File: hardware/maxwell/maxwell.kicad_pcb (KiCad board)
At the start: 2 copper layers, 129.5 x 59.7 mm, 89 parts, among them J1 Canbus 1, J2 Canbus 2, J3 Neopixel, J4 Boot Selection Jumper, J5 Charger Output, J6 Programmer, J7 Dynamo Input, J8 USB Input, J9 Battery, Q1 BSS138, Q2 Q_NMOS_GDS, Q3 Q_PMOS_GDS, U1 MCP2515-E/ST-SOIC, U10 LT1529, U11 TPS2514, U2 SN65HVD233, U3 ITEAD_HC-05, U4 SIM800L_5-pin, U5 BOOST_BOARD, U6 STT3P2UH7, U7 STM32F103RETx, U8 TLP188, U9 Buck Regulator, Y1 16M, Y2 8M, Y3 32.768k

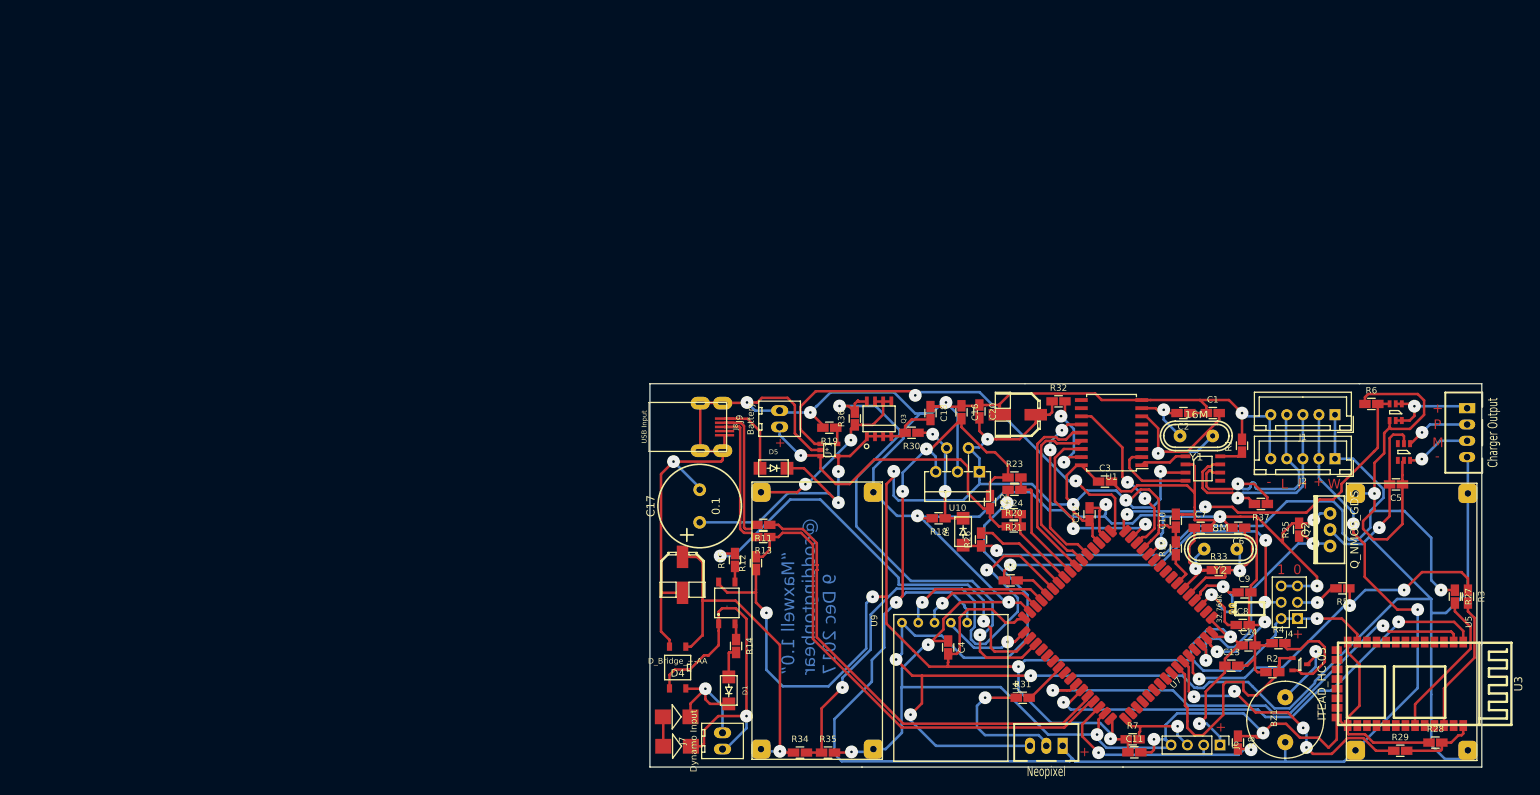
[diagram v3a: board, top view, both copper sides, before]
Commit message: Maxwell Board v2.0;
Adds:

* On-board P-MOS polarity protection.
* Adds On-board GPS (PA6C)
* Adds On-board WIFI, and BLE (ESP32)
* Connectors for 2x external UART devices.
* Connectors for 2x external SPI devices.
* Connector for I2C devices.

Removals:

* Removes on-board GSM; will add later via UART connectors mentioned
  above.
* Removes on-board boost charging.  Can later add this functionality via
  provided connectors.

Changes:

* Although the GNDPWR ground reference still exists, only neopixels
  are switched off via it.  The quiescent current of the GPS module
  and the ESP32 can be controlled via other means.
* Swaps many of the ICs used for switching and power regulation.
* Removes boot jumper bank.  I very rarely used it, and the HC-05
  has now been proven to work for switching boot modes for remote
  flashing.
* Removes natural powered-off state previously handled bydisabling the
  voltage regulator until POWER_ON was pulled high.  This will
  undoubtedly decrease how long the device will be able to operate due
  to increased quiescent currents, but I am willing to accept that given
  that removing that logic makes the design and software (especially
  around keeping the device on while flashing) simpler.
* Many other minor things.
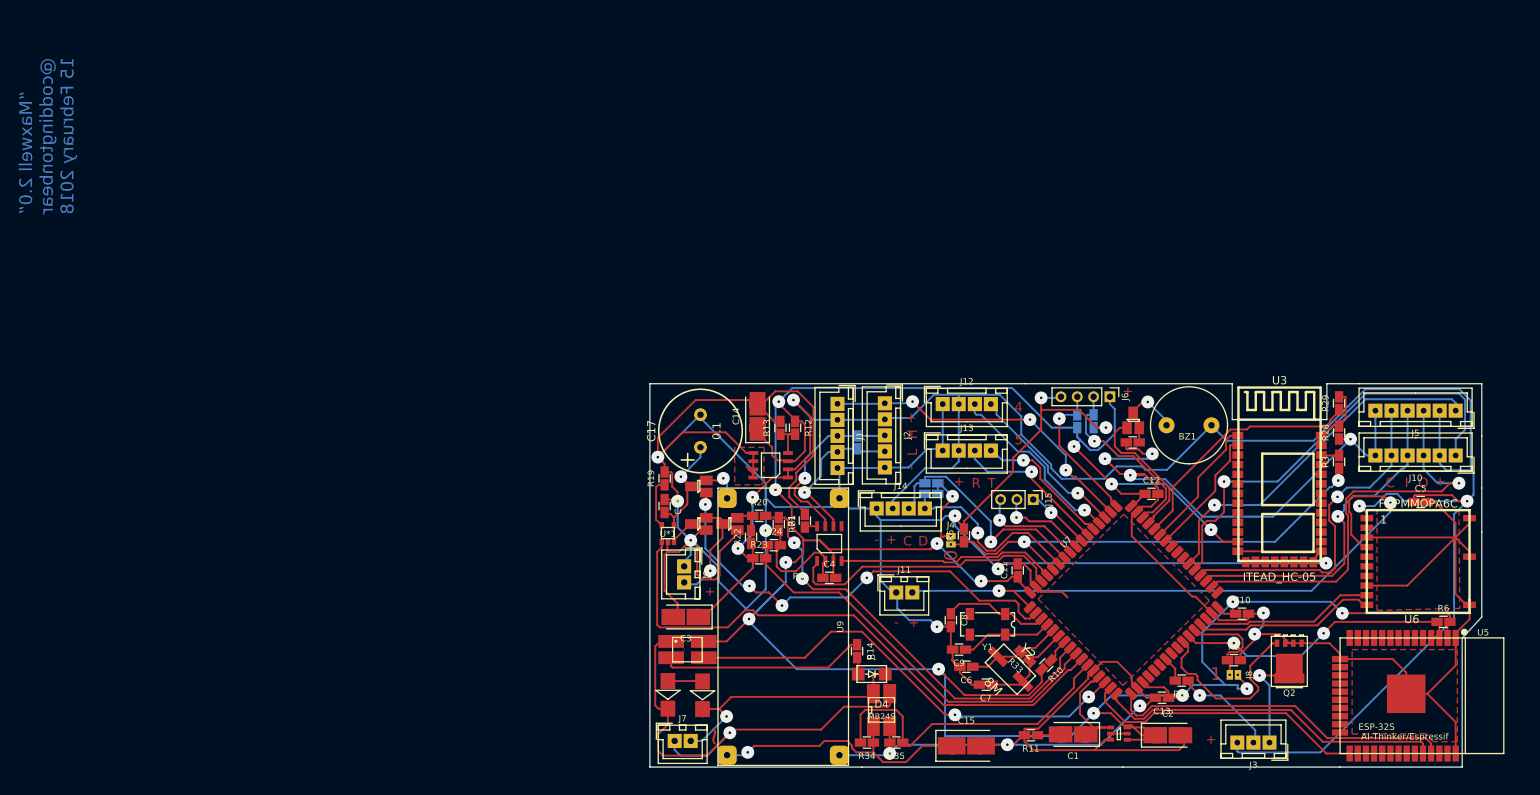
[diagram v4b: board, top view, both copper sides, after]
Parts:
- removed C16: 100nF, coddingtonbear/coddingtonbear.pretty:0805_Milling
- removed C19: 220u, xesscorp/xess.pretty:xess-ECAP-SMT-6.3MM
- removed C20: 100n, coddingtonbear/coddingtonbear.pretty:0805_Milling
- removed D5, D6: D, mcous/kicad-lib/footprints/diode.pretty:DO-214AC
- removed R15: 330, coddingtonbear/coddingtonbear.pretty:0805_Milling
- removed R18, R25: 100k, coddingtonbear/coddingtonbear.pretty:0805_Milling
- removed R26, R27: 1k, coddingtonbear/coddingtonbear.pretty:0805_Milling
- removed R30: 1.5k, coddingtonbear/coddingtonbear.pretty:0805_Milling
- removed R32, R36: 10k, coddingtonbear/coddingtonbear.pretty:0805_Milling
- removed U11: TPS2514, adamgreig/agg-kicad/agg.pretty:SOT-23-6
- removed U4: SIM800L_5-pin, coddingtonbear/coddingtonbear.pretty:SIM800L_Breakout
- removed Y3: 32.768k, f4grx/f4libs_th.pretty:XTAL32K
- added J10: SPI2_B, coddingtonbear/coddingtonbear.pretty:JST_XH_B06B-XH-A_06x2.50mm_Straight_LargePads, F.Cu at (199.1, 82.3)
- added J11: BACKUP, coddingtonbear/coddingtonbear.pretty:JST_XH_B02B-XH-A_02x2.50mm_Straight_LargePads, F.Cu at (112.0, 103.6)
- added J12: UART4, coddingtonbear/coddingtonbear.pretty:JST_XH_B04B-XH-A_04x2.50mm_Straight_LargePads, F.Cu at (119.3, 74.3)
- added J13: UART5, coddingtonbear/coddingtonbear.pretty:JST_XH_B04B-XH-A_04x2.50mm_Straight_LargePads, F.Cu at (119.3, 81.5)
- added J14: I2C1, coddingtonbear/coddingtonbear.pretty:JST_XH_B04B-XH-A_04x2.50mm_Straight_LargePads, F.Cu at (109.0, 90.6)
- added J15: GPIO, KiCad/Pin_Headers.pretty:Pin_Header_Straight_1x03_Pitch2.54mm, F.Cu at (133.3, 89.2)
- added Q4: NTR1P02T1, coddingtonbear/coddingtonbear.pretty:SOT-23_LargePads, F.Cu at (81.3, 93.0)
- added Q5: NTR1P02T1, coddingtonbear/coddingtonbear.pretty:SOT-23_LargePads, F.Cu at (86.1, 93.0)
- added R16: 2.2k, coddingtonbear/coddingtonbear.pretty:0805_Milling, B.Cu at (117.5, 88.3)
- C1, C2: value 22p -> 2.2u; footprint coddingtonbear/coddingtonbear.pretty:0805_Milling -> coddingtonbear:CP_Tantalum_Case-C_EIA-6032-28_Milling
- C14: value 100n -> 220u; footprint coddingtonbear/coddingtonbear.pretty:0805_Milling -> coddingtonbear:CP_Tantalum_Case-C_EIA-6032-28_Milling
- C15: footprint xesscorp/xess.pretty:xess-ECAP-SMT-6.3MM -> coddingtonbear:CP_Tantalum_Case-D_EIA-7343-31_Milling
- C3: value 0.1u -> 2.2u; footprint coddingtonbear/coddingtonbear.pretty:0805_Milling -> coddingtonbear:CP_Tantalum_Case-C_EIA-6032-28_Milling
- D4: value D_Bridge_+-AA -> MB24S; footprint ep092/library_toni.pretty:SO-4 -> coddingtonbear/coddingtonbear.pretty:SO-4_Milling
- J1, J2: footprint KiCad/Connectors_JST.pretty:JST_XH_B05B-XH-A_05x2.50mm_Straight -> coddingtonbear/coddingtonbear.pretty:JST_XH_B05B-XH-A_05x2.50mm_Straight_LargePads
- J3: footprint pbrook/Parts.pretty:JST-XH-3 -> coddingtonbear/coddingtonbear.pretty:JST_XH_B03B-XH-A_03x2.50mm_Straight_LargePads
- J4: value Boot Selection Jumper -> BOOT0; footprint KiCad/Pin_Headers.pretty:Pin_Header_Straight_2x03_Pitch2.54mm -> coddingtonbear:Pin_Header_Straight_1x02_Pitch1.27mm_JMP
- J5: value Charger Output -> SPI2_A; footprint pbrook/Parts.pretty:JST-XH-4 -> coddingtonbear/coddingtonbear.pretty:JST_XH_B06B-XH-A_06x2.50mm_Straight_LargePads
- J7, J9: footprint ChristianLerche/LercheTech_KiCAD/LercheTech.pretty:Lerche_2P_2.54mm_Terminal -> coddingtonbear/coddingtonbear.pretty:JST_XH_B02B-XH-A_02x2.50mm_Straight_LargePads
- J8: value USB Input -> BOOT1; footprint coddingtonbear/coddingtonbear.pretty:UJ2-MIBH-4-SMT -> coddingtonbear:Pin_Header_Straight_1x02_Pitch1.27mm_JMP
- Q1: footprint adamgreig/agg-kicad/agg.pretty:SOT-23 -> coddingtonbear/coddingtonbear.pretty:SOT-23_LargePads
- Q2: value Q_NMOS_GDS -> PSMN5R4-25YLD; footprint fruchti/fruchtilib/mod/to.pretty:TO220 -> coddingtonbear/coddingtonbear.pretty:PSMN5R4-25YLD
- Q3: value Q_PMOS_GDS -> NTR1P02T1; footprint coddingtonbear/coddingtonbear.pretty:NDS8434 -> coddingtonbear/coddingtonbear.pretty:SOT-23_LargePads
- R11: value 20 -> 50
- R12: value 1.5k -> 16-17k
- R13: value 20 -> 10k
- R14: value 330 -> 200
- R2: value 10k -> 2.2k; moved to B.Cu
- R20, R23: value 4.7k -> ANY
- R21, R24: value 10k -> ANY
- R34: value 10k -> 110k
- R35: value 2k -> 10k
- R37, R7, R8: moved to B.Cu
- R6: value 100k -> 10k
- U1: value MCP2515-E/ST-SOIC -> MCP1501; footprint Tinkerforge/kicad-libraries:SOIC-18 -> adamgreig/agg-kicad/agg.pretty:SOT-23-6
- U10: value LT1529 -> MIC39102; footprint KiCad/TO_SOT_Packages_THT.pretty:TO-220-5_Pentawatt_Multiwatt-5_Vertical_StaggeredType2 -> adamgreig/agg-kicad/agg.pretty:SOIC-8
- U5: value BOOST_BOARD -> ESP-32S; footprint coddingtonbear/coddingtonbear.pretty:BOOST_LM2596_3A -> coddingtonbear/coddingtonbear.pretty:ESP-32S
- U6: value STT3P2UH7 -> FGPMMOPA6C; footprint adamgreig/agg-kicad/agg.pretty:SOT-23-6 -> coddingtonbear/coddingtonbear.pretty:FGPMMOPA6C
- U8: footprint Tinkerforge/kicad-libraries:SO-4 -> coddingtonbear/coddingtonbear.pretty:SO-4_Milling
- Y1: value 16M -> 32.768k; footprint SchrodingersGat/Components.pretty:crystal_hc-49s -> KiCad/Crystals.pretty:Crystal_SMD_SeikoEpson_MC306-4pin_8.0x3.2mm
- Y2: footprint SchrodingersGat/Components.pretty:crystal_hc-49s -> nqbit/NQBit.pretty:HC-49USX_SMD
- moved J8 88.5 mm to (165.2, 116.5)
- moved C14 84.4 mm to (90.4, 76.2), turned to 90 degrees
- moved J1 77.5 mm to (102.9, 74.2), turned to 270 degrees
- moved J2 70.6 mm to (110.2, 74.2), turned to 270 degrees
- moved R1 69.1 mm to (97.8, 92.4)
- moved C3 68.6 mm to (79.2, 107.4), turned to 180 degrees
- moved R37 63.6 mm to (105.9, 80.2), turned to 90 degrees
- moved R2 60.7 mm to (117.5, 86.6), turned to 180 degrees
- moved R5 59.5 mm to (122.6, 94.7), turned to 90 degrees
- moved U2 59.3 mm to (101.6, 96.0), turned to 90 degrees
- moved J6 56.9 mm to (145.3, 73.2)
- moved J4 55.5 mm to (120.5, 94.9), turned to 0 degrees
- moved R29 54.9 mm to (181.0, 74.2), turned to 90 degrees
- moved R8 54.9 mm to (142.7, 77.0), turned to 90 degrees
- moved C1 54.6 mm to (139.6, 125.7), turned to 180 degrees
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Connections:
- net RXD renamed BT_DO
- net TXD renamed BT_DI
- C1 pad 1: GND -> Net-(C1-Pad1)
- C2 pad 1: Net-(C2-Pad1) -> +3V3
- C2 pad 2: Net-(C2-Pad2) -> GND
- C3 pad 1: +3V3 -> +BATT
- C5 pad 1: Net-(C5-Pad1) -> +BATT
- C5 pad 2: GNDPWR -> GND
- J3 pad 1: +BATT -> GNDPWR
- J3 pad 3: GNDPWR -> +BATT
- J4 pad 2: +3V3 -> BOOT0
- J5 pad 1: Net-(J5-Pad1) -> SPI2_CS_A
- J5 pad 2: Net-(J5-Pad2) -> +BATT
- J5 pad 3: Net-(J5-Pad3) -> SPI2_MOSI
- J5 pad 4: GNDPWR -> SPI2_MISO
- J8 pad 1: Net-(D5-Pad2) -> +3V3
- J8 pad 2: USB- -> BOOT1
- J9 pad 1: Net-(J9-Pad1) -> GND
- J9 pad 2: GND -> Net-(J9-Pad2)
- Q2 pad 1: ENABLE_BATT_POWER -> GND
- Q2 pad 2: GNDPWR -> ENABLE_BATT_POWER
- Q2 pad 3: GND -> GNDPWR
- Q3 pad 2: /Power/+Dynamo -> Net-(Q3-Pad2)
- Q3 pad 3: Net-(Q3-Pad3) -> /Power/+Dynamo
- R11 pad 1: /Microcontroller/USB_PRER- -> Net-(C1-Pad2)
- R11 pad 2: USB- -> GND
- R12 pad 2: /Microcontroller/USB_PRER+ -> Net-(R12-Pad2)
- R13 pad 1: /Microcontroller/USB_PRER+ -> Net-(R12-Pad2)
- R13 pad 2: USB+ -> GND
- R2 pad 1: GND -> +3V3
- R2 pad 2: BUZZER -> I2C1_SCL
- R20 pad 1: Net-(J9-Pad1) -> Net-(Q5-Pad2)
- R21 pad 2: GNDPWR -> GND
- R22 pad 2: Net-(J9-Pad1) -> Net-(Q5-Pad2)
- R24 pad 2: GNDPWR -> GND
- R5 pad 2: Net-(J4-Pad3) -> GND
- R6 pad 1: Net-(C5-Pad1) -> ~DISABLE_ESP
- R6 pad 2: ~ENABLE_USB_OUT -> +3V3
- R9 pad 1: Net-(J4-Pad4) -> BOOT1
- R9 pad 2: BOOT1 -> GND
- U*1 pad 3: Net-(J9-Pad1) -> Net-(Q4-Pad3)
- U1 pad 1: /TXCAN -> Net-(C1-Pad1)
- U1 pad 2: /RXCAN -> GND
- U1 pad 3: Net-(U1-Pad3) -> GND
- U1 pad 4: Net-(U1-Pad4) -> +3V3
- U1 pad 5: Net-(U1-Pad5) -> GND
- U1 pad 6: Net-(U1-Pad6) -> +3V3
- U10 pad 1: +3V3 -> +BATT
- U10 pad 2: +3V3 -> +BATT
- U10 pad 3: GND -> +3V3
- U10 pad 4: Net-(D6-Pad1) -> Net-(R12-Pad2)
- U10 pad 5: +BATT -> GND
- U2 pad 1: /TXCAN -> CAN_TX
- U2 pad 4: /RXCAN -> CAN_RX
- U5 pad 1: +BATT -> GND
- U5 pad 2: GNDPWR -> +3V3
- U5 pad 3: Net-(C5-Pad1) -> ~DISABLE_ESP
- U5 pad 4: GNDPWR -> Net-(U5-Pad4)
- U6 pad 1: Net-(J5-Pad1) -> +BATT
- U6 pad 3: ~ENABLE_USB_OUT -> GND
- U6 pad 4: Net-(C5-Pad1) -> +BACKUP
- U6 pad 5: Net-(J5-Pad1) -> Net-(U6-Pad5)
- U6 pad 6: Net-(J5-Pad1) -> Net-(U6-Pad6)
- U7 pad 1: +3V3 -> +BACKUP
- U7 pad 10: Net-(U7-Pad10) -> ~BATT_CHARGING
- U7 pad 11: Net-(U7-Pad11) -> DYNAMO_VOLTAGE
- U7 pad 13: +3V3 -> Net-(C1-Pad1)
- U7 pad 14: CAN_INT -> SPEED
- U7 pad 15: ~CAN_CS -> ESP_BOOT_MODE
- U7 pad 16: ~ENABLE_USB_OUT -> ESP_DI
- U7 pad 17: ~BATT_CHARGING -> ESP_DO
- U7 pad 2: Net-(U7-Pad2) -> ~BATT_CHARGE_ENABLE
- U7 pad 21: SCK -> Net-(U7-Pad21)
- U7 pad 22: MISO -> Net-(U7-Pad22)
- U7 pad 23: MOSI -> NEOPIXEL
- U7 pad 24: CURRENT_SENSE -> Net-(U7-Pad24)
- U7 pad 25: BATT_VOLTAGE -> Net-(U7-Pad25)
- U7 pad 26: Net-(R26-Pad2) -> ENABLE_BATT_POWER
- U7 pad 27: DYNAMO_VOLTAGE -> ~DISABLE_ESP
- U7 pad 29: GSM_TXD -> GPS_DI
- U7 pad 30: GSM_RXD -> GPS_DO
- U7 pad 33: GSM_RST -> Net-(U7-Pad33)
- U7 pad 34: SPEED -> SPI2_MOSI
- U7 pad 35: ~BATT_CHARGE_ENABLE -> SPI2_MISO
- U7 pad 36: Net-(U7-Pad36) -> SPI2_SCK
- U7 pad 37: Net-(U7-Pad37) -> SPI2_CS_B
- U7 pad 38: Net-(U7-Pad38) -> SPI2_CS_A
- U7 pad 39: NEOPIXEL -> Net-(U7-Pad39)
- U7 pad 44: /Microcontroller/USB_PRER- -> BT_KEY
- U7 pad 45: /Microcontroller/USB_PRER+ -> BUZZER
- U7 pad 50: Net-(U7-Pad50) -> POWER_ON
- U7 pad 51: Net-(U7-Pad51) -> UART4_TX
- U7 pad 52: Net-(U7-Pad52) -> UART4_RX
- U7 pad 53: Net-(U7-Pad53) -> UART5_TX
- U7 pad 54: Net-(U7-Pad54) -> UART5_RX
- U7 pad 58: BUZZER -> I2C1_SCL
- U7 pad 59: BT_KEY -> I2C1_SDA
- U7 pad 61: Net-(U7-Pad61) -> CAN_RX
- U7 pad 62: ENABLE_BATT_POWER -> CAN_TX
- U7 pad 8: Net-(U7-Pad8) -> BATT_VOLTAGE
- U7 pad 9: Net-(U7-Pad9) -> CURRENT_SENSE
- U8 pad 4: Net-(R15-Pad1) -> SPEED
- U9 pad 3: Net-(Q3-Pad3) -> Net-(Q3-Pad2)
- Y1 pad 1: Net-(C1-Pad2) -> Net-(C8-Pad1)
- Y1 pad 2: Net-(C2-Pad2) -> Net-(Y1-Pad2)
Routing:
- net GNDPWR: track 280.2 -> 20.0 mm, vias 5 -> 1
- net GND: track 639.5 -> 839.4 mm
- net +BACKUP: track 0.00 -> 103.2 mm, vias 0 -> 2
- net /Microcontroller/USB_PRER+: track 77.9 -> 0.00 mm
- net /Microcontroller/USB_PRER-: track 73.1 -> 0.00 mm
- net +3V3: track 381.8 -> 453.0 mm, vias 12 -> 16
- net SPI2_CS_B: track 0.00 -> 70.4 mm, vias 0 -> 1
- net +BATT: track 252.1 -> 321.8 mm
- net SPI2_MOSI: track 0.00 -> 67.6 mm, vias 0 -> 1
- net POWER_ON: track 118.0 -> 51.6 mm, vias 2 -> 3
- net Net-(C5-Pad1): track 60.7 -> 0.00 mm, vias 1 -> 0
- net Net-(J4-Pad4): track 58.3 -> 0.00 mm, vias 3 -> 0
- net SPI2_CS_A: track 0.00 -> 56.6 mm, vias 0 -> 1
- net ~ENABLE_USB_OUT: track 56.5 -> 0.00 mm, vias 2 -> 0
- net BT_DI: track 75.8 -> 20.2 mm, vias 2 -> 0
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- added copper zone on F.Cu, net GND
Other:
- outline, holes or cut-outs redrawn
- net class Default: clearance 0.25 -> 0.2; trace_width 0.4 -> 0.3
- rule trace_clearance: 0.25 -> 0.2
- board text added: "4"
- board text added: "5"
- board text added: "C"
- board text added: "D"
- board text added: "I"
- board text added: "O"
- board text added: "R"
- board text added: "T"
- board text added: "~"
- board text added: "~~"
- board text added: "“Maxwell 2.0” @coddingtonbear 15 February 2018"
- board text removed: "M"
- board text removed: "P"
- board text removed: "W"
- board text removed: "“Maxwell 1.0” @coddingtonbear 9 Dec 2017"

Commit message: Adding label.
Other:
- board text added: "Maxwell v2.0 @coddingtonbear 17 February 2018"
- board text removed: "“Maxwell 2.0” @coddingtonbear 15 February 2018"
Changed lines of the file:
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@@
   (layers
     (0 F.Cu signal)
-    (31 B.Cu signal)
-    (33 F.Adhes user)
-    (35 F.Paste user)
-    (37 F.SilkS user)
-    (39 F.Mask user)
-    (40 Dwgs.User user)
-    (41 Cmts.User user)
-    (42 Eco1.User user)
-    (43 Eco2.User user)
-    (44 Edge.Cuts user)
-    (45 Margin user)
-    (47 F.CrtYd user)
-    (49 F.Fab user)
+    (31 B.Cu signal hide)
+    (33 F.Adhes user hide)
+    (35 F.Paste user hide)
+    (37 F.SilkS user hide)
+    (39 F.Mask user hide)
+    (40 Dwgs.User user hide)
+    (41 Cmts.User user hide)
+    (42 Eco1.User user hide)
+    (43 Eco2.User user hide)
+    (44 Edge.Cuts user hide)
+    (45 Margin user hide)
+    (47 F.CrtYd user hide)
+    (49 F.Fab user hide)
   )
   (setup
@@
     (pad_to_mask_clearance 0.2)
     (aux_axis_origin 73.66 130.81)
-    (visible_elements FFFFFF7F)
+    (visible_elements FFFFFD7F)
     (pcbplotparams
       (layerselection 0x01030_ffffffff)
@@
     (tags "resistor 0805")
     (attr smd)
-    (fp_text reference R5 (at 0 -2.1 90) (layer F.SilkS)
+    (fp_text reference R5 (at 2.286 1.905 90) (layer F.SilkS)
       (effects (font (size 1 1) (thickness 0.15)))
     )
@@
     (effects (font (size 1.5 1.5) (thickness 0.3)))
   )
-  (gr_text "“Maxwell 2.0”\n@coddingtonbear\n15 February 2018" (at -20.2565 44.7675 90) (layer B.Cu)
+  (gr_text "Maxwell v2.0\n@coddingtonbear\n17 February 2018" (at 129.286 110.236) (layer B.Cu)
     (effects (font (size 2 2) (thickness 0.25)) (justify right mirror))
   )

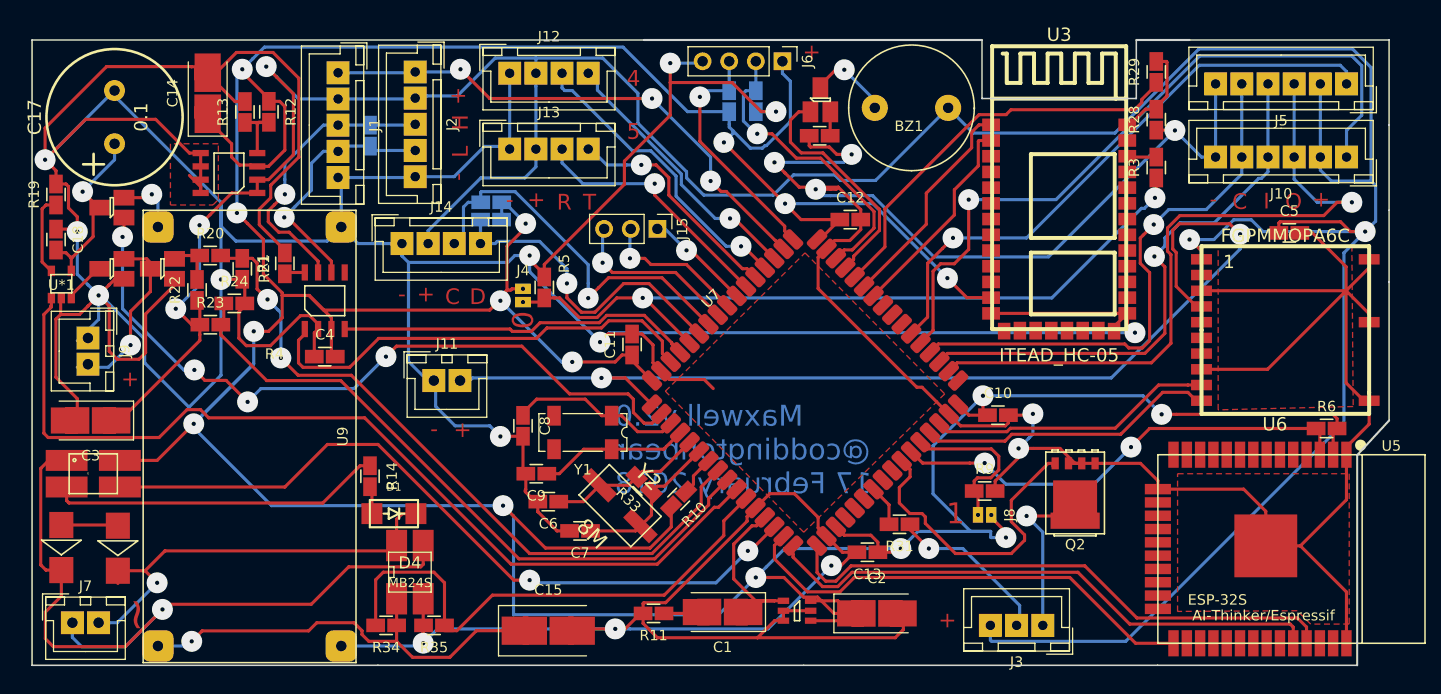
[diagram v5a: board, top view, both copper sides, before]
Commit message: Updating to use 0.4mm traces.
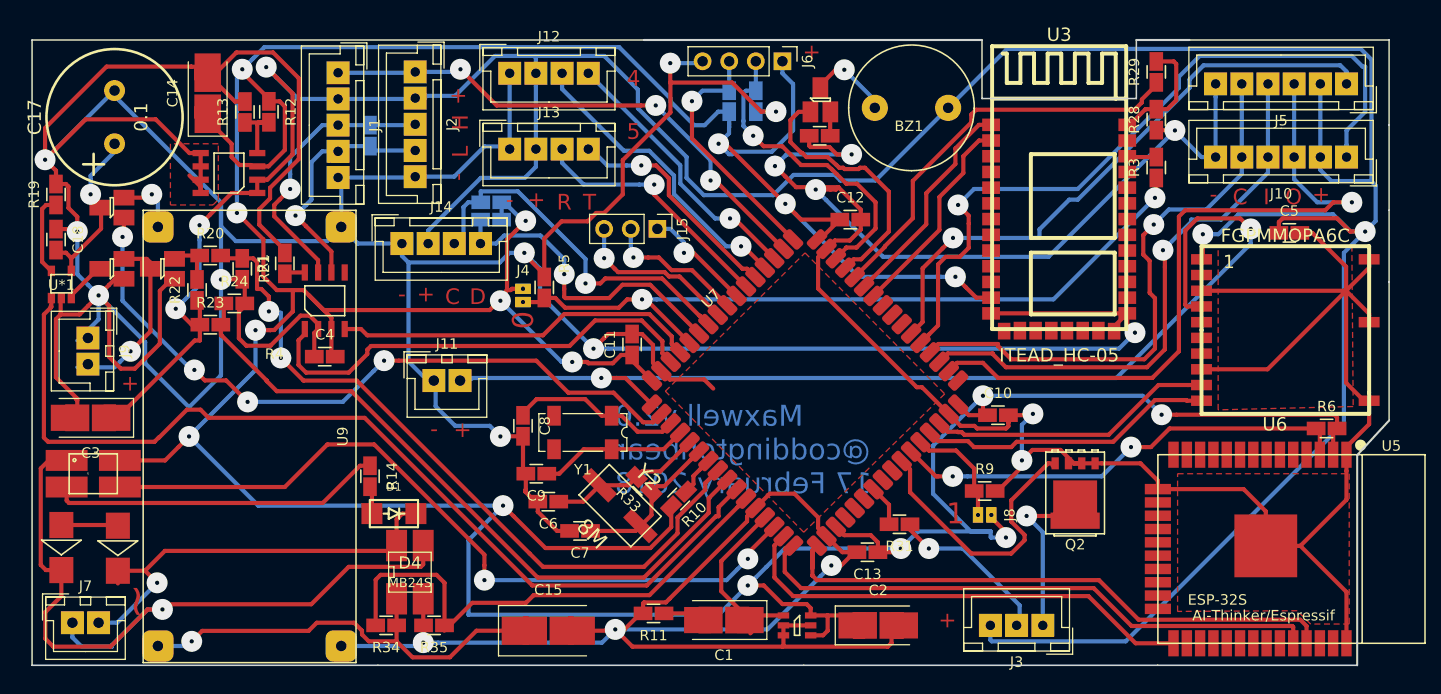
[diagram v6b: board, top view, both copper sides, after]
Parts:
- moved U1 1.40 mm to (146.7, 127.0)
- moved C2 1.15 mm to (154.4, 127.0)
- moved C1 0.77 mm to (139.7, 126.5)
- moved C3 0.25 mm to (79.2, 107.2)
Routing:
- net GND: track 839.4 -> 845.2 mm
- net BOOT1: track 16.0 -> 11.2 mm
- net BUZZER: track 22.4 -> 25.2 mm
- net ~BATT_CHARGING: track 89.8 -> 92.6 mm
- net ENABLE_BATT_POWER: track 29.9 -> 27.5 mm
- net ~BATT_CHARGE_ENABLE: track 70.2 -> 67.8 mm
- net BATT_VOLTAGE: track 68.0 -> 70.2 mm
- net SPI2_CS_B: track 70.4 -> 72.6 mm
- net CURRENT_SENSE: track 63.9 -> 65.9 mm
- net SPI2_SCK: track 52.7 -> 54.7 mm
- net SPI2_MOSI: track 67.6 -> 69.4 mm
- net Net-(R28-Pad2): track 9.35 -> 11.1 mm
- net I2C1_SCL: track 37.1 -> 35.5 mm
- net SPEED: track 71.8 -> 73.4 mm
- net +BATT: track 321.8 -> 320.3 mm
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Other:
- net class Default: trace_width 0.3 -> 0.4
